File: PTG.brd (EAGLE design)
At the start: 105.4 x 82.5 mm, 95 parts, among them IC1 TPS62120, IC2 PIC32MK1024MCF064-I_PT, IC3 LT1762EMS8-5PBF, IC4 TPS561208DDCR, IC5 LT1762EMS8-5PBF, J1 STX-3100-5N, J2 RCJ-01X_PHONO_SINGLE, U4 PCM1748E/2K, X1 22-23-2041, Y1 EXTERNALCRYSTAL

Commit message: correct file upload
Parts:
- removed BATT_HOLDER: BATTERY_HOLDER, BattHolder:HOLDER
- removed BUTTON1, BUTTON2, BUTTON3, BUTTON4: BUTTON-DPDT-7MM, button-dpdt-7mm:BUTTON-DPDT-7MM
- removed DIS1: NHD-0216K3Z-FL-GBW-V3, realdisplay:NHD-0216K3Z-FL-GBW-V3
- removed ENC1: ENCODERENCODER, ENCODER_PTG:ENCODER
- removed IC5: LT1762EMS8-5PBF, LDO:MSOP-8_MS
- removed ROCKER_SW: POWERSWITCH, RockerSwitch:ROCKERVIAS
- removed U4: PCM1748E/2K, PCM1748:DBQ16
- added BH1: BATTERY_HOLDER, Batt_Holder:BATTERY_HOLDER
- added D1: NHD-0216K3Z-GBW-V3, NHD-0216K3Z-FL-GBW-V3:NHD-0216K3Z-FL-GBW-V3
- added IC6, IC7: LT1762, LT1762:MS8
- added J3: 22-27-2021-02, con-molex:6410-02
- added SW1: ROCKER_SWITCH, Rocker_Sw:ROCKER_SWITCH
- added SW2: ENCODER, Encoder:EC12E24204A7
- added SW3, SW4, SW5, SW6: MHPS2273N, Button:MHPS2273N
- C1, C10, C11, C12, C13, C16, C17, C24, C25, C26, C9: device rcl:C0805 -> rcl:C0603K
- C14, C15, C2, C21, C4: device rcl:C0603 -> rcl:C0603K
- C18, C5, C6, C7, C8: device rcl:C0805 -> rcl:C0805K
- C19, C20, C22, C23: device rcl:C0603 -> rcl:C0805K
- C3: value 10uF -> 10nF; device rcl:C0805 -> rcl:C0603K
- IC1: device texas:DCN-R-PDSO-G8 -> TPS62120:SOT23(8)
- IC3: value LT1762EMS8-5PBF -> PCM1748; device LDO:MSOP-8_MS -> PCM1748:SSOP
- IC4: value TPS561208DDCR -> TPS561208; device TPS561208DDCR:SOT95P280X110-6N -> TPS561208:SOT6
- J1: value STX-3100-5N -> STX31005NB; device NewSDR:STX-3100-5N -> STX31005NB:STX31005NB
- J2: value RCJ-01X_PHONO_SINGLE -> RCJ-01X; device RCA:RCA_RA_PCB_SINGLE -> RCJ-01X:RCJ-01X
- L1, L2: device NewSDR:C0603K -> VLCF4020Inductor:VLCF4020
- moved L2 75.5 mm to (51.1, 29.6), turned to 270 degrees
- moved IC3 59.3 mm to (18.2, 70.7), turned to 270 degrees
- moved R2 58.2 mm to (21.8, 7.11)
- moved R6 48.0 mm to (82.8, 7.11)
- moved R4 22.7 mm to (42.2, 7.11)
- moved TP5 19.9 mm to (30.0, 79.8)
- moved TP10 16.0 mm to (19.4, 39.8)
- moved J2 15.5 mm to (1.40, 30.9), turned to 180 degrees
- moved R17 13.5 mm to (36.4, 31.6), turned to 0 degrees
- moved R5 13.1 mm to (62.5, 7.11)
- moved C6 12.8 mm to (43.7, 32.9)
- moved C19 12.6 mm to (30.7, 30.0), turned to 180 degrees
- moved C22 12.4 mm to (50.8, 33.3)
- moved TP1 12.0 mm to (19.4, 35.9)
- moved R15 11.4 mm to (36.6, 33.1), turned to 0 degrees
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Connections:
- removed net +5_DAC: C17.1, C2.1, C3.1, IC5.1, IC5.2, R26.2, TP4.1, TP4.TP, U4.6
- removed net 5V_I/O: C20.1, C21.1, IC1.4, IC1.8, IC3.5, IC3.8, IC5.5, IC5.8, L1.2, R15.2, R18.2, R24.2, TP1.1, TP1.TP
- removed net PWR_PIN: ROCKER_SW.1
- removed net SW-B: BATT_HOLDER.+, ROCKER_SW.3
- removed net VOUT_LCD: C4.1, C5.1, DIS1.J1-3, DIS1.J2-6, IC3.1, IC3.2, R25.2, TP3.1, TP3.TP
- new net +5V5: C20.1, C21.1, IC1.4, IC1.8, IC6.5, IC6.8, IC7.5, IC7.8, L1.2, R15.2, R18.2, R24.2, TP1.1, TP1.TP
- new net +5V_DAC: C17.1, C2.1, C3.1, IC3.6, IC6.1, IC6.2, R26.2, TP4.1, TP4.TP
- new net +5V_LCD: C4.1, C5.1, D1.3, D1.9, IC7.1, IC7.2, R25.2, TP3.1, TP3.TP
- new net N$29: BH1.POS, SW1.1
- new net N$30: J3.2, SW1.3
- net !DAC_CS: now also IC3.15; no longer U4.15
- net +3V3: now also IC3.5, SW3.2, SW3.5, SW4.2, SW4.5, SW5.2, SW5.5, SW6.2, SW6.5; no longer BUTTON1.2, BUTTON1.5, BUTTON2.2, BUTTON2.5, BUTTON3.2, BUTTON3.5, BUTTON4.2, BUTTON4.5, U4.5
- net AGND: now also IC3.4, IC3.9, IC6.4; no longer IC5.4, U4.4, U4.9
- net BUTTON1: now also SW3.3, SW3.4; no longer BUTTON1.3, BUTTON1.4
- net BUTTON2: now also SW4.3, SW4.4; no longer BUTTON2.3, BUTTON2.4
- net BUTTON3: now also SW5.3, SW5.4; no longer BUTTON3.3, BUTTON3.4
- net BUTTON4: now also SW6.3, SW6.4; no longer BUTTON4.3, BUTTON4.4
- net DAC_BCK: now also IC3.1; no longer U4.1
- net DAC_DATA: now also IC3.2; no longer U4.2
- net DAC_LRCK: now also IC3.3; no longer U4.3
- net DAC_SPI_CLK: now also IC3.14; no longer U4.14
- net DAC_SPI_DATA: now also IC3.13; no longer U4.13
- net DAC_ZEROH: now also IC3.11; no longer U4.11
- net DAC_ZEROL: now also IC3.12; no longer U4.12
- net DIS_!CS: now also D1.4; no longer DIS1.J2-1
- net DIS_SCK: now also D1.6; no longer DIS1.J2-3
- net DIS_SDI: now also D1.7; no longer DIS1.J2-4
- net ENC_A: now also SW2.A; no longer ENC1.PIN_A
- net ENC_B: now also SW2.B; no longer ENC1.PIN_B
- net GND: now also BH1.NEG, D1.2, D1.8, D1.G1, D1.G2, D1.G3, D1.G4, IC7.4, J2.3, J2.4, J3.1, SW1.G1, SW1.G2, SW2.C, SW2.G1, SW2.G2; no longer BATT_HOLDER.-, DIS1.J1-2, DIS1.J2-5, DIS1.M1, DIS1.M2, DIS1.M3, DIS1.M4, ENC1.PIN_C, IC3.4, J2.1', J2.1''
- net N$19: now also IC3.10; no longer U4.10
- net N$23: now also IC7.3; no longer IC3.3
- net N$9: now also IC6.3; no longer IC5.3
- net SIGNAL_L: now also IC3.7; no longer U4.7
- net SIGNAL_R: now also IC3.8; no longer U4.8
- net SUPPLY: now also SW1.2; no longer ROCKER_SW.2
- net SYS_CLK: now also IC3.16; no longer U4.16
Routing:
- net +5V5: track 0.00 -> 125.4 mm, vias 0 -> 10
- net 5V_I/O: track 120.1 -> 0.00 mm, vias 6 -> 0
- net PWR_PIN: track 55.6 -> 0.00 mm, vias 3 -> 0
- net BUTTON1: track 37.4 -> 79.6 mm
- net N$30: track 0.00 -> 37.4 mm
- net BUTTON4: track 65.8 -> 40.2 mm, vias 1 -> 2
- net BUTTON2: track 37.9 -> 61.4 mm, vias 2 -> 1
- net VOUT_LCD: track 21.0 -> 0.00 mm
- net +5V_LCD: track 0.00 -> 18.3 mm
- net +3V3: track 45.6 -> 27.4 mm, vias 48 -> 32
- net SW-B: track 15.8 -> 0.00 mm
- net SUPPLY: track 50.2 -> 65.5 mm, vias 4 -> 0
- net GND: track 43.3 -> 29.2 mm, vias 73 -> 79
- net BUTTON3: track 52.6 -> 40.4 mm, vias 1 -> 2
- net N$29: track 0.00 -> 12.1 mm
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- added copper zone on layer 1, net +5V5
- added copper zone on layer 1, net +5V_DAC
- added copper zone on layer 1, net +5V_LCD
- removed copper zone on layer 1, net +5_DAC
- removed copper zone on layer 1, net 5V_I/O
- removed copper zone on layer 16, net GND
- removed copper zone on layer 1, net VOUT_LCD
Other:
- board text added: "5V5"
- board text added: "LCD LDO Out"
- board text removed: "+"
- board text removed: "-"
- board text removed: "LDO"

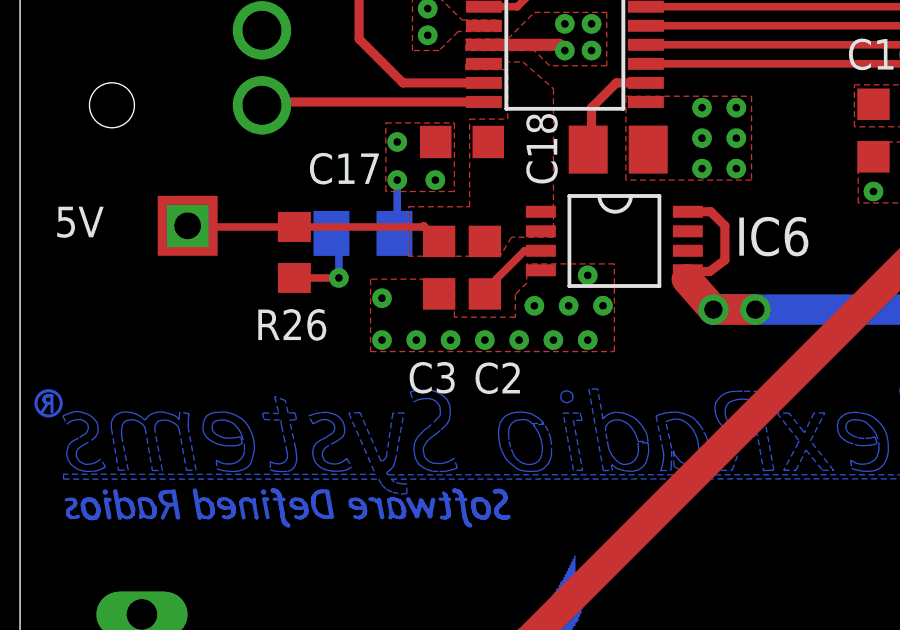
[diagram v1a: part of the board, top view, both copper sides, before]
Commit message: fixed 10uF cap on IC6
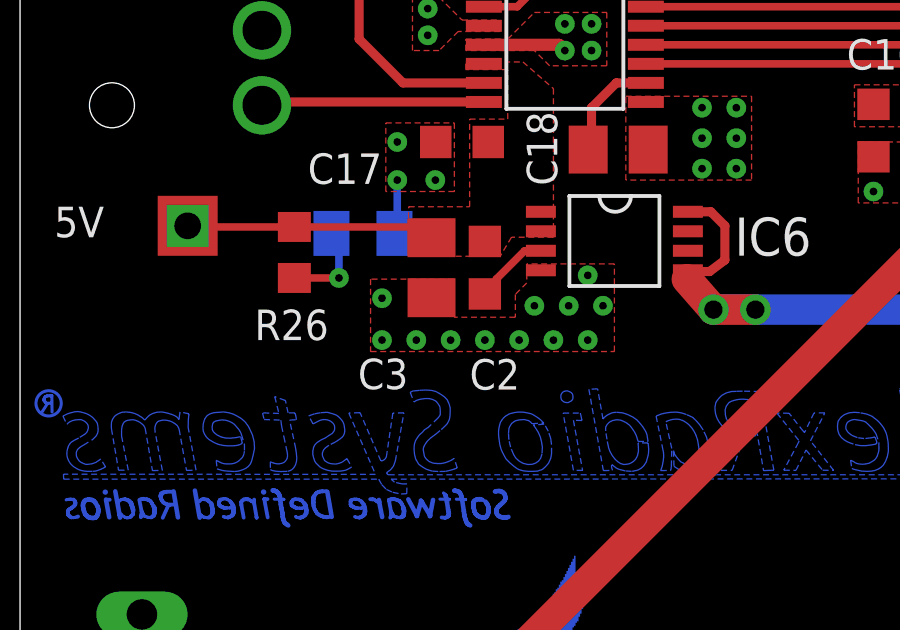
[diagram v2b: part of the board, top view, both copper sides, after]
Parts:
- C3: value 10nF -> 10uF; device rcl:C0603K -> rcl:C0805K
- moved C3 0.25 mm to (13.7, 63.0)
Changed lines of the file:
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@@
 </element>
 <element name="C2" library="rcl" package="C0603K" value="10nF" x="15.494" y="62.992" smashed="yes" rot="R270">
-<attribute name="NAME" x="15.113" y="58.801" size="1.016" layer="25" font="vector"/>
+<attribute name="NAME" x="14.986" y="58.928" size="1.016" layer="25" font="vector"/>
 <attribute name="VALUE" x="13.589" y="63.627" size="1.27" layer="27" rot="R270"/>
 </element>
@@
 <attribute name="NAME" x="5.144" y="81.265" size="1.27" layer="26" font="vector" rot="MR180"/>
 </element>
-<element name="C3" library="rcl" package="C0603K" value="10nF" x="13.97" y="62.992" smashed="yes" rot="R270">
-<attribute name="NAME" x="12.916" y="58.816" size="1.016" layer="25" font="vector"/>
-<attribute name="VALUE" x="12.32" y="63.792" size="1.016" layer="27" rot="R270"/>
+<element name="C3" library="rcl" package="C0805K" value="10uF" x="13.716" y="62.992" smashed="yes" rot="R270">
+<attribute name="NAME" x="11.265" y="58.943" size="1.016" layer="25" font="vector"/>
+<attribute name="VALUE" x="12.066" y="63.792" size="1.016" layer="27" rot="R270"/>
 </element>
 <element name="J3" library="con-molex" package="6410-02" value="22-27-2021-02" x="4.064" y="50.165" smashed="yes" rot="MR90">
@@
 <wire x1="13.423" y1="64.35" x2="13.462" y2="64.389" width="0.254" layer="1"/>
 <wire x1="13.462" y1="64.389" x2="13.462" y2="64.375" width="0.254" layer="1"/>
-<wire x1="13.462" y1="64.375" x2="13.97" y2="63.867" width="0.254" layer="1"/>
+<wire x1="13.462" y1="64.375" x2="13.716" y2="63.992" width="0.254" layer="1"/>
 <wire x1="9.144" y1="64.35" x2="5.627" y2="64.35" width="0.254" layer="1"/>
 <wire x1="5.627" y1="64.35" x2="5.588" y2="64.389" width="0.254" layer="1"/>
